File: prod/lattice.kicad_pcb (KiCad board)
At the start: 2 copper layers, 114.3 x 81 mm, 69 parts

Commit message: schematic pretty solid
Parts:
- B1, B2: value (none) -> SW_SPST; footprint SW_SPST -> project:SW_SPST_SKQG_WithStem
- C1, C2, C3: value (none) -> 100n; footprint 100n -> project:C_0603_1608Metric
- D1, D10, D11, D12, D13, D14, D15, D16, D17, D18, D19, D2, D20, D21, D22, D23, D24, D3, D4, D5, D6, D7, D8, D9: value (none) -> 1N4148W; footprint 1N4148W -> project:D_SOD-123_via
- F1, F2: value (none) -> 500mA; footprint 500mA -> project:Fuse_0603_1608Metric
- J1, J2: value (none) -> USB_C_Receptacle; footprint USB_C_Receptacle -> project:USB_C_Receptacle_HRO_TYPE-C-31-M-12
- MX1, MX10, MX11, MX12, MX13, MX14, MX15, MX16, MX17, MX18, MX19, MX2, MX20, MX21, MX22, MX23, MX24, MX3, MX4, MX5, MX6, MX7, MX8, MX9: value (none) -> MX_SW_HS; footprint MX_SW_HS -> project:SW_MX_HS_S_1u
- R1, R2, R5, R6: value (none) -> 5k1; footprint 5k1 -> project:R_0603_1608Metric
- R3: value (none) -> 330R; footprint 330R -> project:R_0603_1608Metric
- R4: value (none) -> 10k; footprint 10k -> project:R_0603_1608Metric
- SW1, SW2, SW3: value (none) -> SW_Slide_DPDT; footprint SW_Slide_DPDT -> project:K3_1390S
- SYM1: value (none) -> Logo_Open_Hardware_Small; footprint Logo_Open_Hardware_Small -> project:OSHW-Logo_5.7x6mm_SilkScreen
- U1: value (none) -> CH552T; footprint CH552T -> project:TSSOP-20_4.4x6.5mm_P0.65mm
- U2: value (none) -> USBLC6-2SC6; footprint USBLC6-2SC6 -> project:SOT-23-6
- moved C2 1.22 mm to (135.3, 50.1)
- moved C3 1.12 mm to (135.3, 51.6)
- moved R2 0.40 mm to (104.8, 44.6)
- moved R6 0.40 mm to (181.0, 44.6)
- moved R3 0.20 mm to (126.3, 67.7)
- moved R1 0.20 mm to (104.8, 46.1)
- moved R5 0.20 mm to (181.0, 46.1)
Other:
- net class Default removed

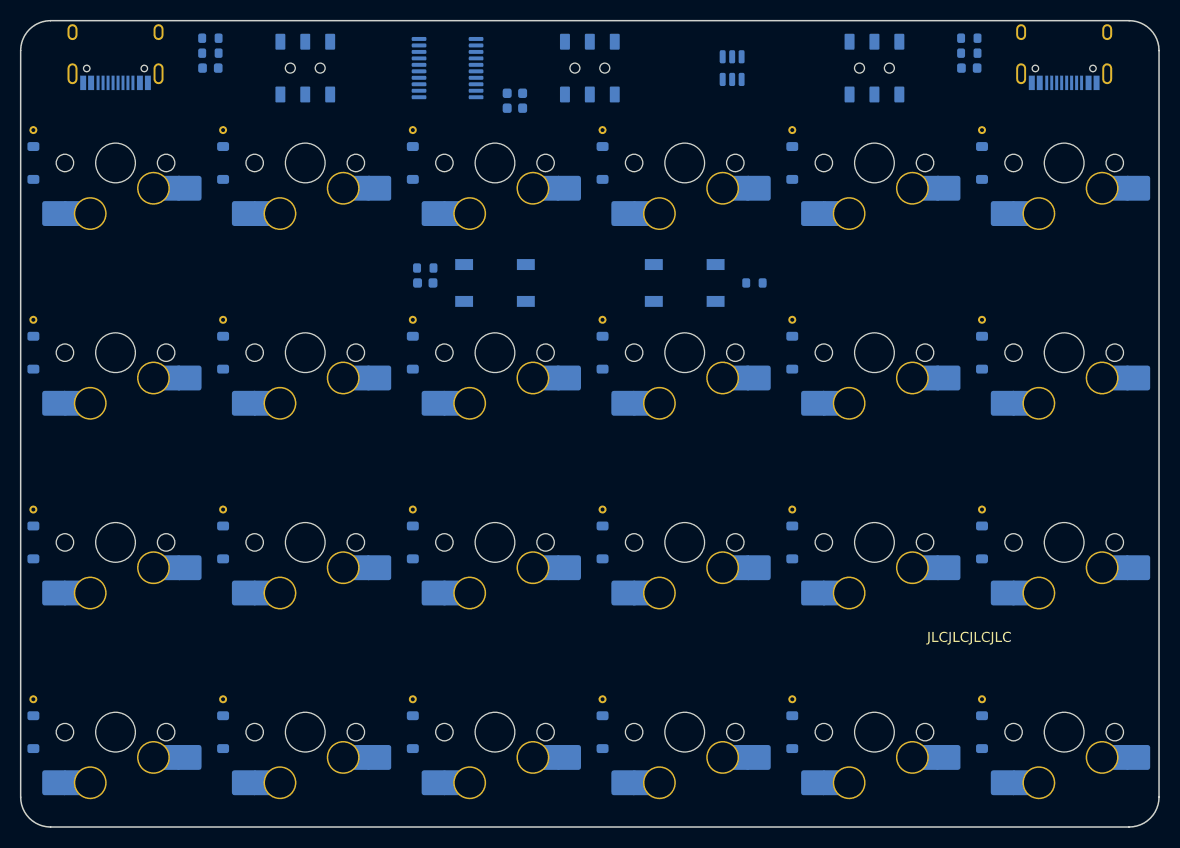
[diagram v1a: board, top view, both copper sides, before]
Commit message: 4 channel mux/demux
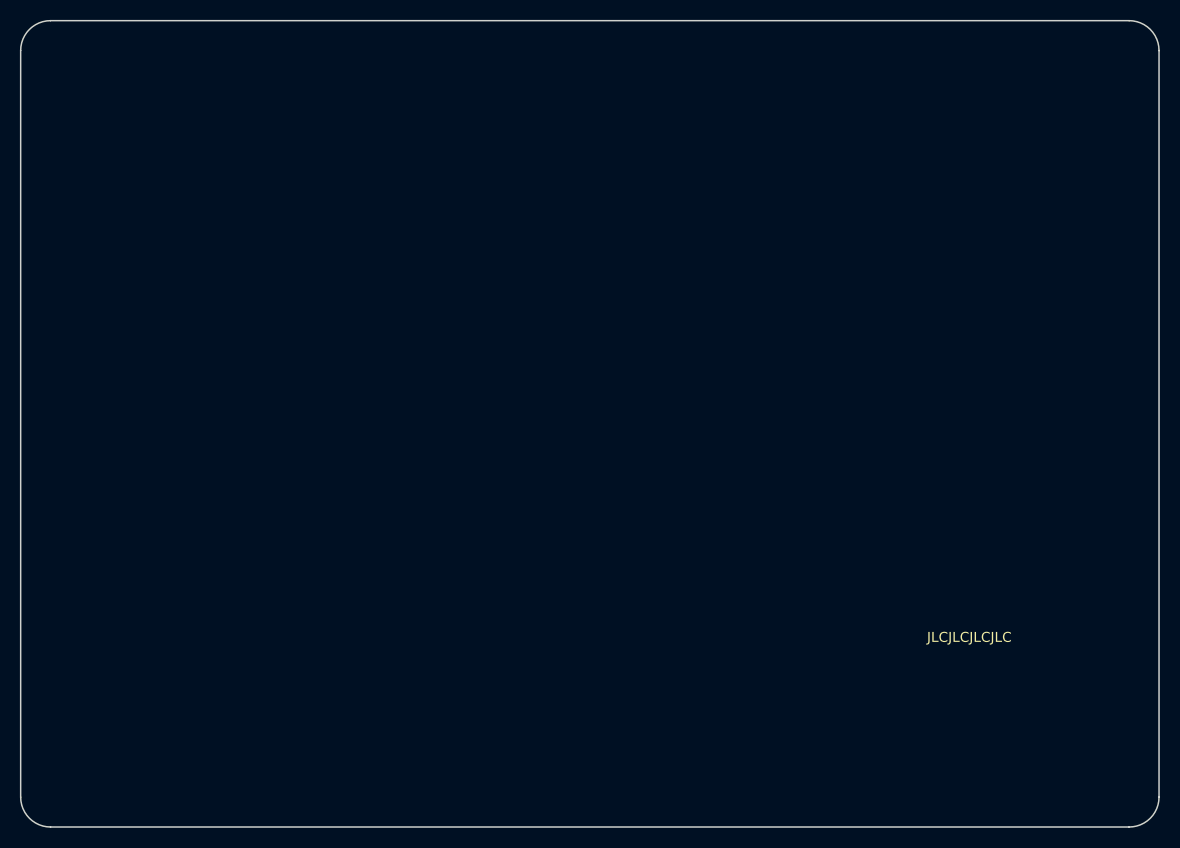
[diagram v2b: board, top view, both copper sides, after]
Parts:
- removed SW2, SW3: SW_Slide_DPDT, project:K3_1390S
- added C4: , 100n, B.Cu at (126.3, 69.2)
- added R7: , 10k, B.Cu at (159.4, 69.2)
- added U3: , USBLC6-2SC6, B.Cu at (114.3, 47.6)
- added U4: , USBLC6-2SC6, B.Cu at (171.4, 47.6)
- B1, B2: value SW_SPST -> (none); footprint project:SW_SPST_SKQG_WithStem -> SW_SPST
- C1, C2: value 100n -> (none); footprint project:C_0603_1608Metric -> 100n
- C3: value 100n -> (none); footprint project:C_0603_1608Metric -> 0.1uF
- D1, D10, D11, D12, D13, D14, D15, D16, D17, D18, D19, D2, D20, D21, D22, D23, D24, D3, D4, D5, D6, D7, D8, D9: value 1N4148W -> (none); footprint project:D_SOD-123_via -> 1N4148W
- F1, F2: value 500mA -> (none); footprint project:Fuse_0603_1608Metric -> 500mA
- J1, J2: value USB_C_Receptacle -> (none); footprint project:USB_C_Receptacle_HRO_TYPE-C-31-M-12 -> USB_C_Receptacle
- MX1, MX10, MX11, MX12, MX13, MX14, MX15, MX16, MX17, MX18, MX19, MX2, MX20, MX21, MX22, MX23, MX24, MX3, MX4, MX5, MX6, MX7, MX8, MX9: value MX_SW_HS -> (none); footprint project:SW_MX_HS_S_1u -> MX_SW_HS
- R1: value 5k1 -> (none); footprint project:R_0603_1608Metric -> 10k
- R2, R5: value 5k1 -> (none); footprint project:R_0603_1608Metric -> 5k1
- R3: value 330R -> (none); footprint project:R_0603_1608Metric -> 5k1
- R4: value 10k -> (none); footprint project:R_0603_1608Metric -> 5k1
- R6: value 5k1 -> (none); footprint project:R_0603_1608Metric -> 330R
- SW1: value SW_Slide_DPDT -> (none); footprint project:K3_1390S -> SW_SPDT
- SYM1: value Logo_Open_Hardware_Small -> (none); footprint project:OSHW-Logo_5.7x6mm_SilkScreen -> Logo_Open_Hardware_Small
- U1: value CH552T -> (none); footprint project:TSSOP-20_4.4x6.5mm_P0.65mm -> CH552T
- U2: value USBLC6-2SC6 -> (none); footprint project:SOT-23-6 -> TS3A44159PWR
- moved R6 59.3 mm to (126.3, 67.7), turned to 180 degrees
- moved R1 47.9 mm to (152.4, 51.7)
- moved R3 31.6 mm to (104.8, 44.6), turned to 0 degrees
- moved R4 31.6 mm to (181.0, 46.1)
- moved SW1 28.7 mm to (142.9, 45.0)
- moved C1 20.3 mm to (133.3, 50.2)
- moved C3 17.1 mm to (152.4, 50.2)
- moved C2 2.50 mm to (133.3, 51.7)
- moved U1 2.24 mm to (126.3, 47.6)
- moved U2 2.24 mm to (159.4, 47.6), turned to 0 degrees
- moved R2 1.50 mm to (104.8, 46.1)
- moved R5 1.50 mm to (181.0, 44.6)
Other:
- net class Default added: clearance 0.2, trace_width 0.25, via_dia 0.8, via_drill 0.4
